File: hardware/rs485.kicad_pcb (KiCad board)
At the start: 2 copper layers, 40 x 40 mm, 50 parts, among them P1 CON-SENSOR2, P2 BOOT, P3 CONN_5, SW1 SW_DIP_4, U1 XMC1XXX48, U2 DRILL, U3 DRILL, U4 DRILL, U5 DRILL, U6 SP3491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

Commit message: specify new rs485 biasing resistors
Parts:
- R3, R5, R6, R8: value 10k -> 2.7k
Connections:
- P1 pad 1: Net-(P1-Pad1) -> (no net)
- RP1 pad 1: Net-(RP1-Pad1) -> (no net)
- RP1 pad 8: Net-(RP1-Pad8) -> (no net)
- RP3 pad 4: Net-(RP3-Pad4) -> (no net)
- U1 pad 10: Net-(U1-Pad10) -> (no net)
- U1 pad 11: Net-(U1-Pad11) -> (no net)
- U1 pad 12: Net-(U1-Pad12) -> (no net)
- U1 pad 2: Net-(U1-Pad2) -> (no net)
- U1 pad 21: Net-(U1-Pad21) -> (no net)
- U1 pad 22: Net-(U1-Pad22) -> (no net)
- U1 pad 26: Net-(U1-Pad26) -> (no net)
- U1 pad 28: Net-(U1-Pad28) -> (no net)
- U1 pad 29: Net-(U1-Pad29) -> (no net)
- U1 pad 3: Net-(U1-Pad3) -> (no net)
- U1 pad 30: Net-(U1-Pad30) -> (no net)
- U1 pad 31: Net-(U1-Pad31) -> (no net)
- U1 pad 32: Net-(U1-Pad32) -> (no net)
- U1 pad 33: Net-(U1-Pad33) -> (no net)
- U1 pad 34: Net-(U1-Pad34) -> (no net)
- U1 pad 35: Net-(U1-Pad35) -> (no net)
- U1 pad 36: Net-(U1-Pad36) -> (no net)
- U1 pad 39: Net-(U1-Pad39) -> (no net)
- U1 pad 4: Net-(U1-Pad4) -> (no net)
- U1 pad 40: Net-(U1-Pad40) -> (no net)
- U1 pad 43: Net-(U1-Pad43) -> (no net)
- U1 pad 44: Net-(U1-Pad44) -> (no net)
- U1 pad 45: Net-(U1-Pad45) -> (no net)
- U1 pad 5: Net-(U1-Pad5) -> (no net)
- U1 pad 6: Net-(U1-Pad6) -> (no net)
- U1 pad 7: Net-(U1-Pad7) -> (no net)
- U1 pad 8: Net-(U1-Pad8) -> (no net)
- U1 pad 9: Net-(U1-Pad9) -> (no net)
- U6 pad 1: Net-(U6-Pad1) -> (no net)
- U6 pad 13: Net-(U6-Pad13) -> (no net)
- U6 pad 8: Net-(U6-Pad8) -> (no net)

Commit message: fix weee logo
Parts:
- VAL: value WEEE_7mm_back -> WEEE_7mm; footprint kicad-libraries:WEEE_7mm_back -> kicad-libraries:WEEE_7mm
- turned VAL to 180 degrees

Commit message: specify processor
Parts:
- U1: value XMC1XXX48 -> XMC1404
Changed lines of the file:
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@@
     (aux_axis_origin 125.3 123.1)
     (grid_origin 125.3 123.1)
-    (visible_elements FFFF7FFF)
+    (visible_elements FFFEFFFF)
     (pcbplotparams
       (layerselection 0x010f8_80000001)
@@
       (effects (font (size 0.29972 0.29972) (thickness 0.0762)))
     )
-    (fp_text value XMC1XXX48 (at 0 -0.7 180) (layer F.SilkS)
+    (fp_text value XMC1404 (at 0 -0.7 180) (layer F.SilkS)
       (effects (font (size 0.29972 0.29972) (thickness 0.0762)))
     )

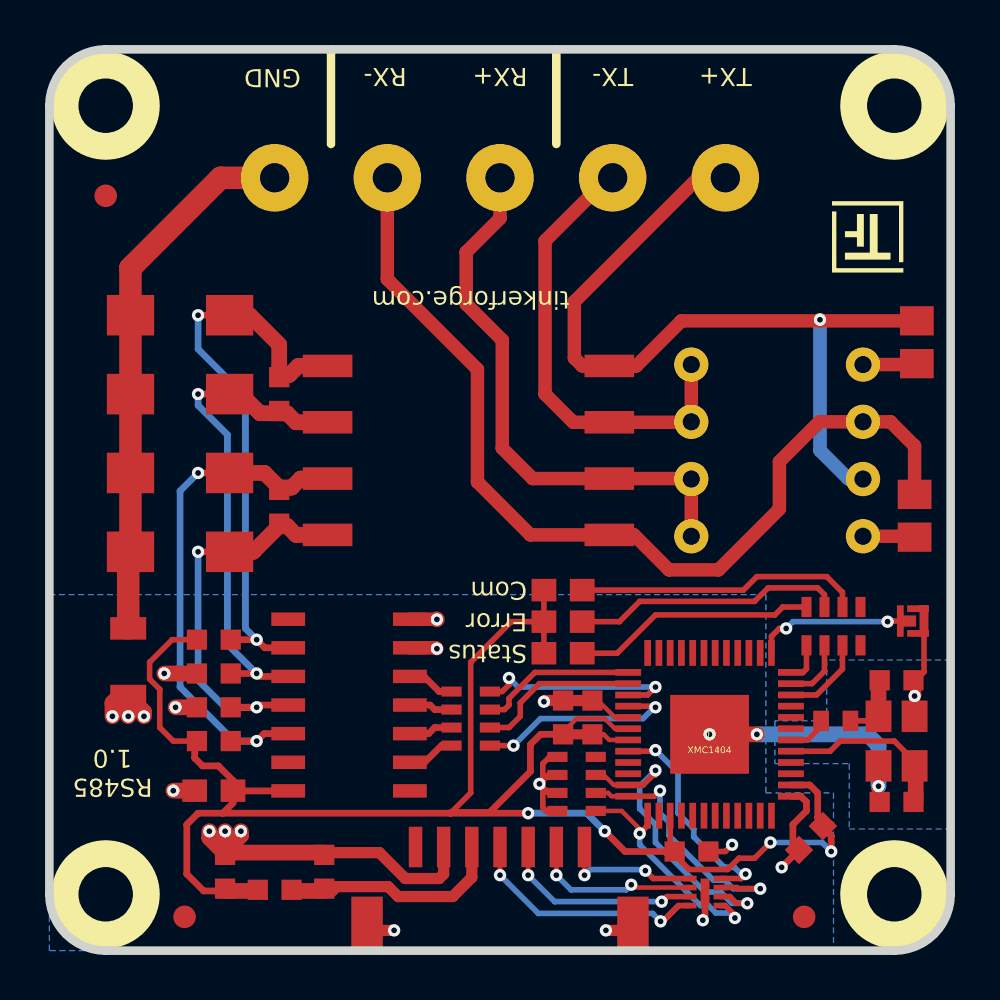
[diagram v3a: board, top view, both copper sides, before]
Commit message: version 1.1
 change SPI filter design
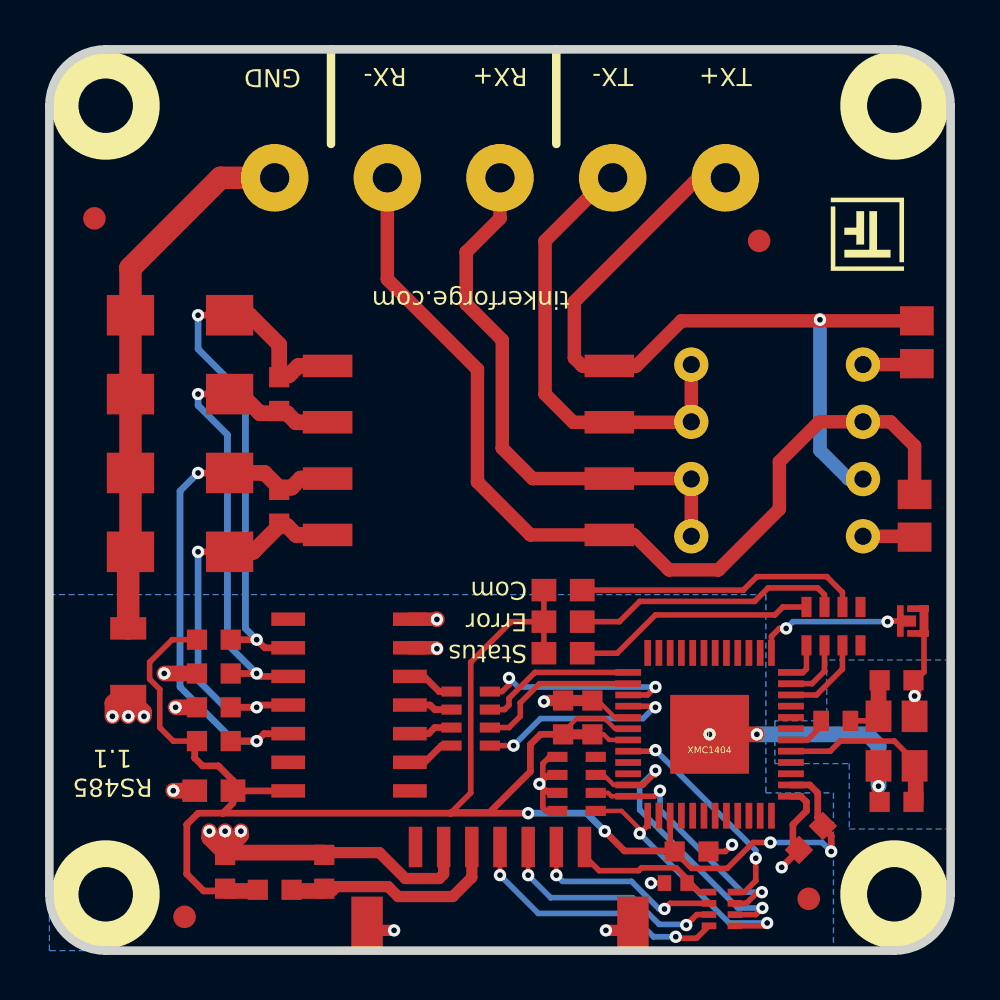
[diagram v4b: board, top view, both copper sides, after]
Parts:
- removed FILTER1: Filter-4x, kicad-libraries:DFN8-17x135
- removed the Fiducial_Mark at (158.8, 121.6)
- removed the Fiducial_Mark at (127.8, 89.6)
- added C101: 220pF, kicad-libraries:C0402F, F.Cu at (153.1, 120.1)
- added Fiducial_Mark: VAL**, kicad-libraries:Fiducial_Mark, F.Cu at (156.8, 91.6)
- added Fiducial_Mark: VAL**, kicad-libraries:Fiducial_Mark, F.Cu at (159.0, 120.8)
- added Fiducial_Mark: VAL**, kicad-libraries:Fiducial_Mark, F.Cu at (127.3, 90.6)
- added RP101: 82, kicad-libraries:4X0402, F.Cu at (155.2, 121.2)
- FB1: footprint C0603F -> kicad-libraries:R0603F
- G***: value Logo_31x31 -> LOGO
- moved G*** 2.33 mm to (161.6, 91.3)
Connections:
- P1 pad 1: (no net) -> Net-(P1-Pad1)
- RP1 pad 1: (no net) -> Net-(RP1-Pad1)
- RP1 pad 8: (no net) -> Net-(RP1-Pad8)
- RP3 pad 4: (no net) -> Net-(RP3-Pad4)
- U1 pad 10: (no net) -> Net-(U1-Pad10)
- U1 pad 11: (no net) -> Net-(U1-Pad11)
- U1 pad 12: (no net) -> Net-(U1-Pad12)
- U1 pad 2: (no net) -> Net-(U1-Pad2)
- U1 pad 21: (no net) -> Net-(U1-Pad21)
- U1 pad 22: (no net) -> Net-(U1-Pad22)
- U1 pad 26: (no net) -> Net-(U1-Pad26)
- U1 pad 28: (no net) -> Net-(U1-Pad28)
- U1 pad 29: (no net) -> Net-(U1-Pad29)
- U1 pad 3: (no net) -> Net-(U1-Pad3)
- U1 pad 30: (no net) -> Net-(U1-Pad30)
- U1 pad 31: (no net) -> Net-(U1-Pad31)
- U1 pad 32: (no net) -> Net-(U1-Pad32)
- U1 pad 33: (no net) -> Net-(U1-Pad33)
- U1 pad 34: (no net) -> Net-(U1-Pad34)
- U1 pad 35: (no net) -> Net-(U1-Pad35)
- U1 pad 36: (no net) -> Net-(U1-Pad36)
- U1 pad 39: (no net) -> Net-(U1-Pad39)
- U1 pad 4: (no net) -> Net-(U1-Pad4)
- U1 pad 40: (no net) -> Net-(U1-Pad40)
- U1 pad 43: (no net) -> Net-(U1-Pad43)
- U1 pad 44: (no net) -> Net-(U1-Pad44)
- U1 pad 45: (no net) -> Net-(U1-Pad45)
- U1 pad 5: (no net) -> Net-(U1-Pad5)
- U1 pad 6: (no net) -> Net-(U1-Pad6)
- U1 pad 7: (no net) -> Net-(U1-Pad7)
- U1 pad 8: (no net) -> Net-(U1-Pad8)
- U1 pad 9: (no net) -> Net-(U1-Pad9)
- U6 pad 1: (no net) -> Net-(U6-Pad1)
- U6 pad 13: (no net) -> Net-(U6-Pad13)
- U6 pad 8: (no net) -> Net-(U6-Pad8)
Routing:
- net S-CS: track 10.4 -> 12.4 mm
- net Net-(P1-Pad5): track 9.00 -> 10.2 mm
- net Net-(P1-Pad6): track 7.59 -> 8.75 mm
- net GND: track 59.8 -> 59.1 mm
- net Net-(C101-Pad1): track 6.19 -> 6.81 mm, vias 2 -> 0
- net S-MOSI: track 12.0 -> 11.4 mm
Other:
- board text added: "RS485 1.1"
- board text removed: "RS485 1.0"

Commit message: update stuff
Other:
- board text added: "Copyright Tinkerforge GmbH 2021. This documentation describes Open Hardware and is licensed under the CERN OHL v. 1.1. You may redistribute and modify this documentation under the terms of the CERN OHL v.1.1. (http://ohwr.org/cernohl). This documentation is distributed WITHOUT ANY EXPRESS OR IMPLIED WARRANTY, INCLUDING OF MERCHANTABILITY, SATISFACTORY QUALITY AND FITNESS FOR A PARTICULAR PURPOSE.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"
- board text removed: "Copyright Tinkerforge GmbH 2015. This documentation describes Open Hardware and is licensed under the CERN OHL v. 1.1. You may redistribute and modify this documentation under the terms of the CERN OHL v.1.1. (http://ohwr.org/cernohl). This documentation is distributed WITHOUT ANY EXPRESS OR IMPLIED WARRANTY, INCLUDING OF MERCHANTABILITY, SATISFACTORY QUALITY AND FITNESS FOR A PARTICULAR PURPOSE.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"

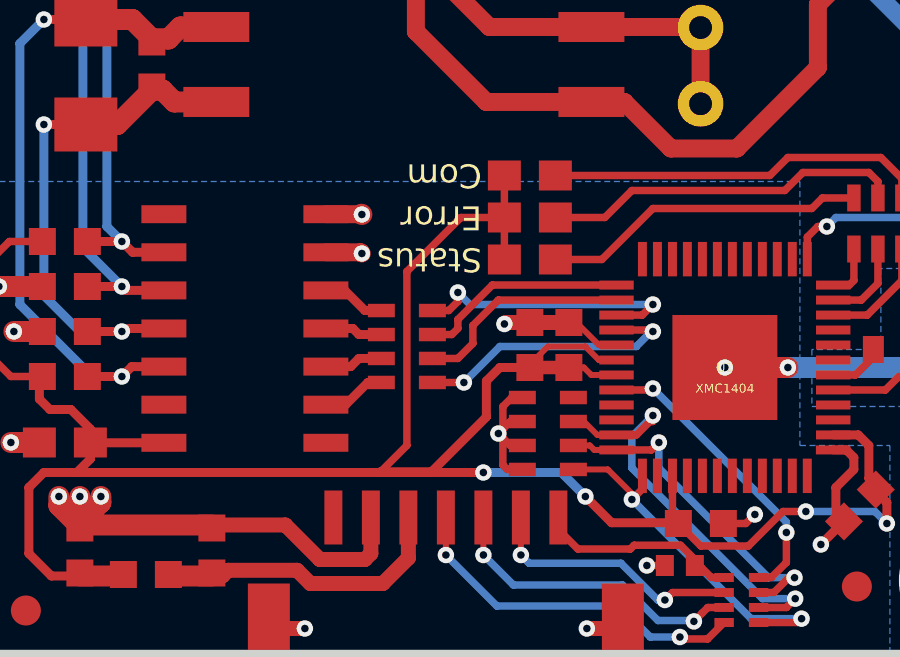
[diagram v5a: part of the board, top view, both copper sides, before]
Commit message: add DE pulldown
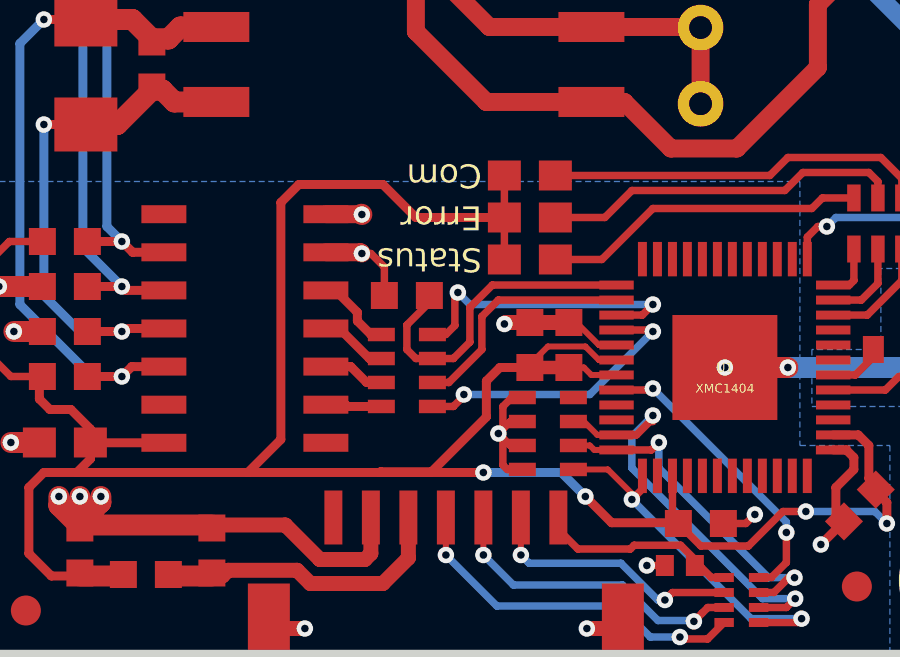
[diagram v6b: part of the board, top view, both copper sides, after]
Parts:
- added R101: 10k, R0603F, F.Cu at (144.0, 111.1)
- moved RP2 0.80 mm to (144.0, 113.6)
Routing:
- net VCC: track 83.7 -> 90.3 mm
- net 485-DE: track 7.00 -> 10.9 mm
- net GND: track 59.1 -> 61.0 mm
- net 485-~REB: track 7.30 -> 7.92 mm
- net Net-(RP2-Pad5): track 2.13 -> 2.68 mm

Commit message: specify part
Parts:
- PTC1: value PTC 0.45A -> 0ZCJ0016FF2E
